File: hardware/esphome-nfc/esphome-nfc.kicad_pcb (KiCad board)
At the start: 4 copper layers, 68.2 x 41 mm, 51 parts, among them SW1 TS-1187A-B-A-B, U1 ESP32-C3-WROOM-02, U2 PN7160A1HN/C100Y, U3 AP2112K-3.3TRG1, U4 USBLC6-2P6, Y1 Crystal_GND24

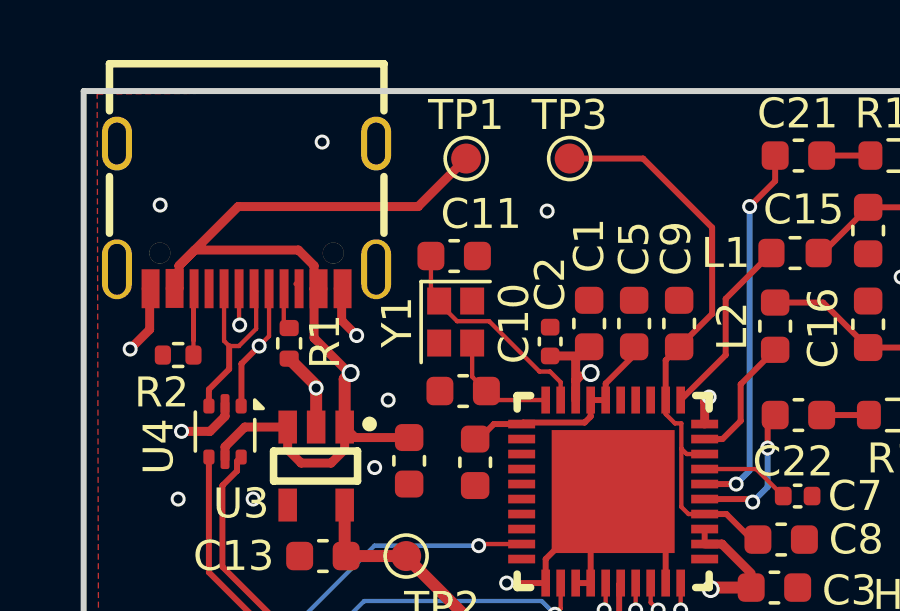
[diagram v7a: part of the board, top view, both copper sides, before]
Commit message: Bump the capacitance of capacitors near the oscillator based on some reading
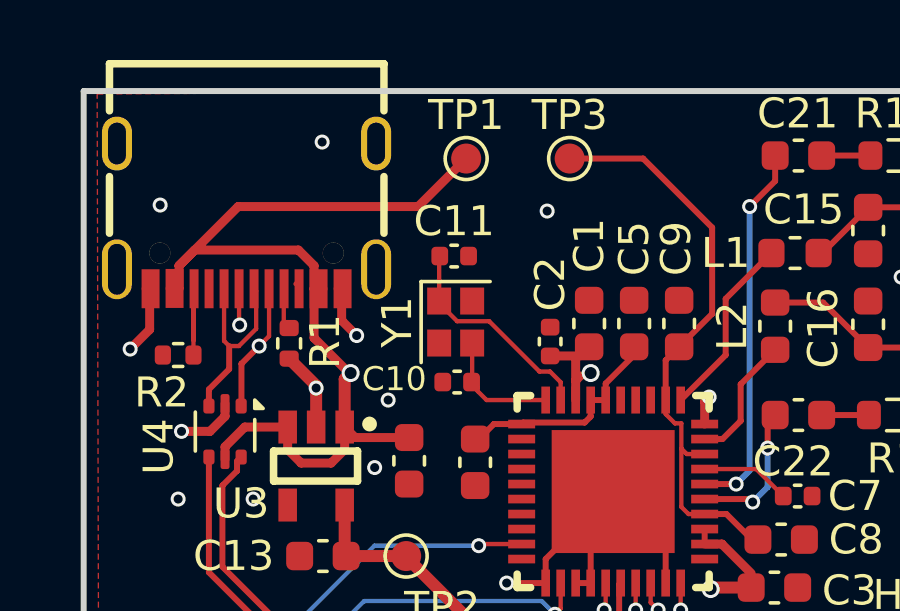
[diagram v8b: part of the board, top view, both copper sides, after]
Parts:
- C10, C11: value 10 pF -> 12 pF; footprint Capacitor_SMD:C_0603_1608Metric -> Capacitor_SMD:C_0402_1005Metric
- moved C10 0.36 mm to (168.7, 83.7)
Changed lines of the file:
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@@
 		)
 	)
-	(footprint "Capacitor_SMD:C_0603_1608Metric"
+	(footprint "Capacitor_SMD:C_0402_1005Metric"
 		(layer "F.Cu")
-		(at 168.9 84 180)
-		(descr "Capacitor SMD 0603 (1608 Metric), square (rectangular) end terminal, IPC_7351 nominal, (Body size source: IPC-SM-782 page 76, https://www.pcb-3d.com/wordpress/wp-content/uploads/ipc-sm-782a_amendment_1_and_2.pdf), generated with kicad-footprint-generator")
+		(at 168.7 83.7 180)
+		(descr "Capacitor SMD 0402 (1005 Metric), square (rectangular) end terminal, IPC_7351 nominal, (Body size source: IPC-SM-782 page 76, https://www.pcb-3d.com/wordpress/wp-content/uploads/ipc-sm-782a_amendment_1_and_2.pdf), generated with kicad-footprint-generator")
 		(tags "capacitor")
 		(property "Reference" "C10"
-			(at -1.7 2.25 90)
+			(at 2.1 0.1 180)
 			(layer "F.SilkS")
 			(effects
 				(font
-					(size 1 1)
+					(size 0.8 0.8)
 					(thickness 0.15)
 				)
 			)
 		)
-		(property "Value" "10 pF"
-			(at 0 1.43 180)
+		(property "Value" "12 pF"
+			(at 0 1.16 180)
 			(layer "F.Fab")
 			(effects
@@
 			)
 		)
-		(property "Footprint" "Capacitor_SMD:C_0603_1608Metric"
+		(property "Footprint" "Capacitor_SMD:C_0402_1005Metric"
 			(at 0 0 180)
 			(unlocked yes)
@@
 			)
 		)
-		(property "LCSC" "C1634"
+		(property "LCSC" "C1547"
 			(at 0 0 180)
 			(unlocked yes)
@@
 		(attr smd)
 		(fp_line
-			(start -0.14058 0.51)
-			(end 0.14058 0.51)
+			(start -0.107836 0.36)
+			(end 0.107836 0.36)
 			(stroke
 				(width 0.12)
@@
 		)
 		(fp_line
-			(start -0.14058 -0.51)
-			(end 0.14058 -0.51)
+			(start -0.107836 -0.36)
+			(end 0.107836 -0.36)
 			(stroke
 				(width 0.12)
@@
 		)
 		(fp_line
-			(start 1.48 0.73)
-			(end -1.48 0.73)
+			(start 0.91 0.46)
+			(end -0.91 0.46)
 			(stroke
 				(width 0.05)
@@
 		)
 		(fp_line
-			(start 1.48 -0.73)
-			(end 1.48 0.73)
+			(start 0.91 -0.46)
+			(end 0.91 0.46)
 			(stroke
 				(width 0.05)
@@
 		)
 		(fp_line
-			(start -1.48 0.73)
-			(end -1.48 -0.73)
+			(start -0.91 0.46)
+			(end -0.91 -0.46)
 			(stroke
 				(width 0.05)
@@
 		)
 		(fp_line
-			(start -1.48 -0.73)
-			(end 1.48 -0.73)
+			(start -0.91 -0.46)
+			(end 0.91 -0.46)
 			(stroke
 				(width 0.05)
@@
 		)
 		(fp_line
-			(start 0.8 0.4)
-			(end -0.8 0.4)
+			(start 0.5 0.25)
+			(end -0.5 0.25)
 			(stroke
 				(width 0.1)
@@
 		)
 		(fp_line
-			(start 0.8 -0.4)
-			(end 0.8 0.4)
+			(start 0.5 -0.25)
+			(end 0.5 0.25)
 			(stroke
 				(width 0.1)
@@
 		)
 		(fp_line
-			(start -0.8 0.4)
-			(end -0.8 -0.4)
+			(start -0.5 0.25)
+			(end -0.5 -0.25)
 			(stroke
 				(width 0.1)
@@
 		)
 		(fp_line
-			(start -0.8 -0.4)
-			(end 0.8 -0.4)
+			(start -0.5 -0.25)
+			(end 0.5 -0.25)
 			(stroke
 				(width 0.1)
@@
 			(effects
 				(font
-					(size 0.4 0.4)
-					(thickness 0.06)
+					(size 0.25 0.25)
+					(thickness 0.04)
 				)
 			)
 		)
 		(pad "1" smd roundrect
-			(at -0.775 0 180)
-			(size 0.9 0.95)
+			(at -0.48 0 180)
+			(size 0.56 0.62)
 			(layers "F.Cu" "F.Paste" "F.Mask")
 			(roundrect_rratio 0.25)
@@
 		)
 		(pad "2" smd roundrect
-			(at 0.775 0 180)
-			(size 0.9 0.95)
+			(at 0.48 0 180)
+			(size 0.56 0.62)
 			(layers "F.Cu" "F.Paste" "F.Mask")
 			(roundrect_rratio 0.25)
@@
 			(pintype "passive")
 		)
-		(model "${KICAD8_3DMODEL_DIR}/Capacitor_SMD.3dshapes/C_0603_1608Metric.wrl"
+		(model "${KICAD8_3DMODEL_DIR}/Capacitor_SMD.3dshapes/C_0402_1005Metric.wrl"
 			(offset
 				(xyz 0 0 0)
@@
 		)
 	)
-	(footprint "Capacitor_SMD:C_0603_1608Metric"
+	(footprint "Capacitor_SMD:C_0402_1005Metric"
 		(layer "F.Cu")
 		(at 168.6 79.5)
-		(descr "Capacitor SMD 0603 (1608 Metric), square (rectangular) end terminal, IPC_7351 nominal, (Body size source: IPC-SM-782 page 76, https://www.pcb-3d.com/wordpress/wp-content/uploads/ipc-sm-782a_amendment_1_and_2.pdf), generated with kicad-footprint-generator")
+		(descr "Capacitor SMD 0402 (1005 Metric), square (rectangular) end terminal, IPC_7351 nominal, (Body size source: IPC-SM-782 page 76, https://www.pcb-3d.com/wordpress/wp-content/uploads/ipc-sm-782a_amendment_1_and_2.pdf), generated with kicad-footprint-generator")
 		(tags "capacitor")
 		(property "Reference" "C11"
-			(at 0.9 -1.4 0)
+			(at 0 -1.16 0)
 			(layer "F.SilkS")
 			(effects
@@
 			)
 		)
-		(property "Value" "10 pF"
-			(at 0 1.43 0)
+		(property "Value" "12 pF"
+			(at 0 1.16 0)
 			(layer "F.Fab")
 			(effects
@@
 			)
 		)
-		(property "Footprint" "Capacitor_SMD:C_0603_1608Metric"
+		(property "Footprint" "Capacitor_SMD:C_0402_1005Metric"
 			(at 0 0 0)
 			(unlocked yes)
@@
 			)
 		)
-		(property "LCSC" "C1634"
+		(property "LCSC" "C1547"
 			(at 0 0 0)
 			(unlocked yes)
@@
 		(attr smd)
 		(fp_line
-			(start -0.14058 -0.51)
-			(end 0.14058 -0.51)
+			(start -0.107836 -0.36)
+			(end 0.107836 -0.36)
 			(stroke
 				(width 0.12)
@@
 		)
 		(fp_line
-			(start -0.14058 0.51)
-			(end 0.14058 0.51)
+			(start -0.107836 0.36)
+			(end 0.107836 0.36)
 			(stroke
 				(width 0.12)
@@
 		)
 		(fp_line
-			(start -1.48 -0.73)
-			(end 1.48 -0.73)
+			(start -0.91 -0.46)
+			(end 0.91 -0.46)
 			(stroke
 				(width 0.05)
@@
 		)
 		(fp_line
-			(start -1.48 0.73)
-			(end -1.48 -0.73)
+			(start -0.91 0.46)
+			(end -0.91 -0.46)
 			(stroke
 				(width 0.05)
@@
 		)
 		(fp_line
-			(start 1.48 -0.73)
-			(end 1.48 0.73)
+			(start 0.91 -0.46)
+			(end 0.91 0.46)
 			(stroke
 				(width 0.05)
@@
 		)
 		(fp_line
-			(start 1.48 0.73)
-			(end -1.48 0.73)
+			(start 0.91 0.46)
+			(end -0.91 0.46)
 			(stroke
 				(width 0.05)
@@
 		)
 		(fp_line
-			(start -0.8 -0.4)
-			(end 0.8 -0.4)
+			(start -0.5 -0.25)
+			(end 0.5 -0.25)
 			(stroke
 				(width 0.1)
@@
 		)
 		(fp_line
-			(start -0.8 0.4)
-			(end -0.8 -0.4)
+			(start -0.5 0.25)
+			(end -0.5 -0.25)
 			(stroke
 				(width 0.1)
@@
 		)
 		(fp_line
-			(start 0.8 -0.4)
-			(end 0.8 0.4)
+			(start 0.5 -0.25)
+			(end 0.5 0.25)
 			(stroke
 				(width 0.1)
@@
 		)
 		(fp_line
-			(start 0.8 0.4)
-			(end -0.8 0.4)
+			(start 0.5 0.25)
+			(end -0.5 0.25)
 			(stroke
 				(width 0.1)
@@
 			(effects
 				(font
-					(size 0.4 0.4)
-					(thickness 0.06)
+					(size 0.25 0.25)
+					(thickness 0.04)
 				)
 			)
 		)
 		(pad "1" smd roundrect
-			(at -0.775 0)
-			(size 0.9 0.95)
+			(at -0.48 0)
+			(size 0.56 0.62)
 			(layers "F.Cu" "F.Paste" "F.Mask")
 			(roundrect_rratio 0.25)
@@
 		)
 		(pad "2" smd roundrect
-			(at 0.775 0)
-			(size 0.9 0.95)
+			(at 0.48 0)
+			(size 0.56 0.62)
 			(layers "F.Cu" "F.Paste" "F.Mask")
 			(roundrect_rratio 0.25)
@@
 			(pintype "passive")
 		)
-		(model "${KICAD8_3DMODEL_DIR}/Capacitor_SMD.3dshapes/C_0603_1608Metric.wrl"
+		(model "${KICAD8_3DMODEL_DIR}/Capacitor_SMD.3dshapes/C_0402_1005Metric.wrl"
 			(offset
 				(xyz 0 0 0)
@@
 	)
 	(segment
-		(start 171.795 83.35)
-		(end 171.445 83.35)
+		(start 168.1 79.52)
+		(end 168.12 79.5)
 		(width 0.145)
 		(layer "F.Cu")
@@
 	)
 	(segment
-		(start 167.825 80.575)
-		(end 167.825 79.5)
+		(start 171.795 83.35)
+		(end 171.445 83.35)
 		(width 0.145)
 		(layer "F.Cu")
@@
 	(segment
 		(start 168.1 81)
-		(end 168.1 80.85)
+		(end 168.1 79.52)
 		(width 0.145)
 		(layer "F.Cu")
@@
 	)
 	(segment
-		(start 168.1 80.85)
-		(end 167.825 80.575)
-		(width 0.145)
-		(layer "F.Cu")
-		(net 26)
-	)
-	(segment
 		(start 171.445 83.35)
 		(end 169.7675 81.6725)
@@
 	(segment
 		(start 171.65 84.3)
-		(end 169.975 84.3)
+		(end 169.68 84.3)
 		(width 0.145)
 		(layer "F.Cu")
@@
 	)
 	(segment
-		(start 169.675 84)
-		(end 169.2 83.525)
+		(start 169.38 83.88)
+		(end 169.2 83.7)
 		(width 0.145)
 		(layer "F.Cu")
@@
 	)
 	(segment
-		(start 169.975 84.3)
-		(end 169.675 84)
+		(start 169.68 84.3)
+		(end 169.38 84)
 		(width 0.145)
 		(layer "F.Cu")
@@
 	)
 	(segment
-		(start 169.2 83.525)
+		(start 169.2 83.7)
 		(end 169.2 82.4)
 		(width 0.145)
 		(layer "F.Cu")
+		(net 34)
+	)
+	(segment
+		(start 169.38 84)
+		(end 169.38 83.88)
+		(width 0.145)
+		(layer "F.Cu")
